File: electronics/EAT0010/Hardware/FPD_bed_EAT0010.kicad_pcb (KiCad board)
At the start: 2 copper layers, 29.2 x 48.2 mm, 20 parts, among them CN1 CONN_02X08, CN2 OSTTA060161, Q1 IPD30N03S4L-09, U1 MIC5205-5.0MB5, U2 PIC16F1704

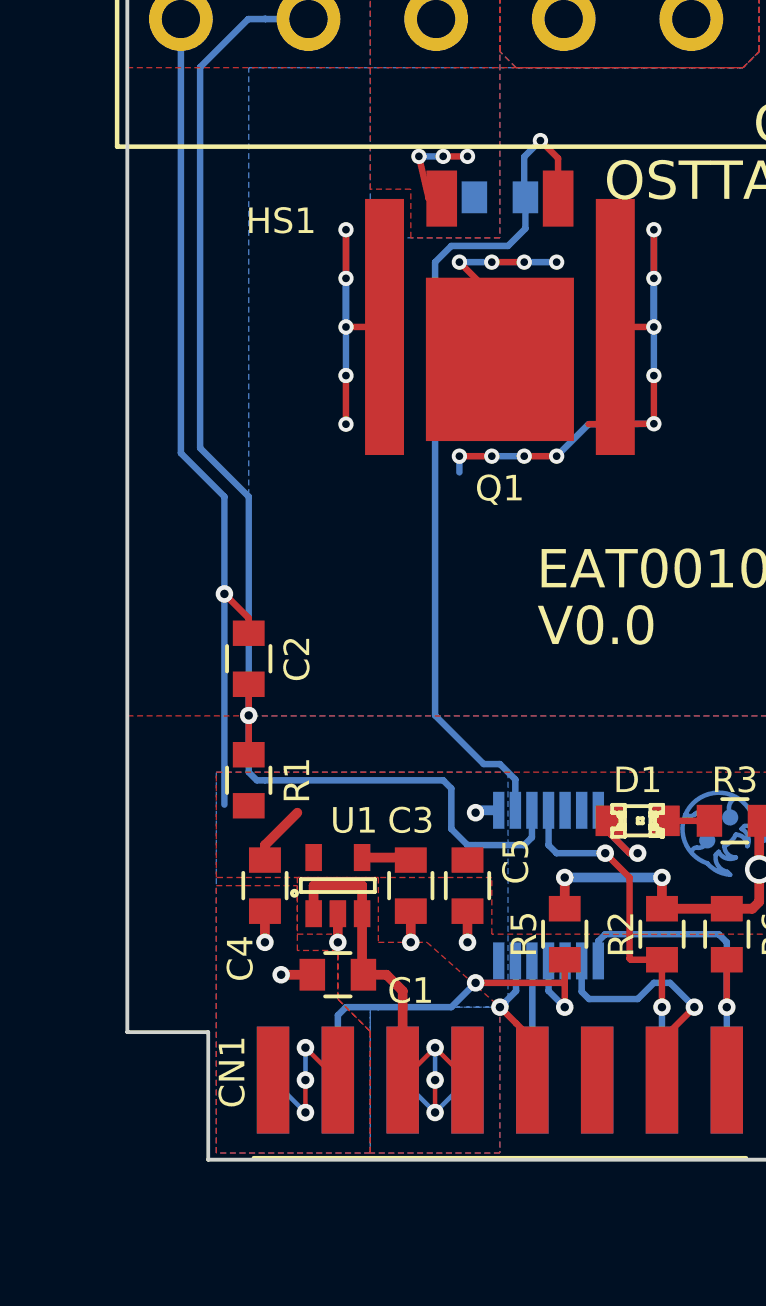
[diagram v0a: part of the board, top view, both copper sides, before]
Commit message: PCB updates
Added thermals and slid parts around a bit for better spacing
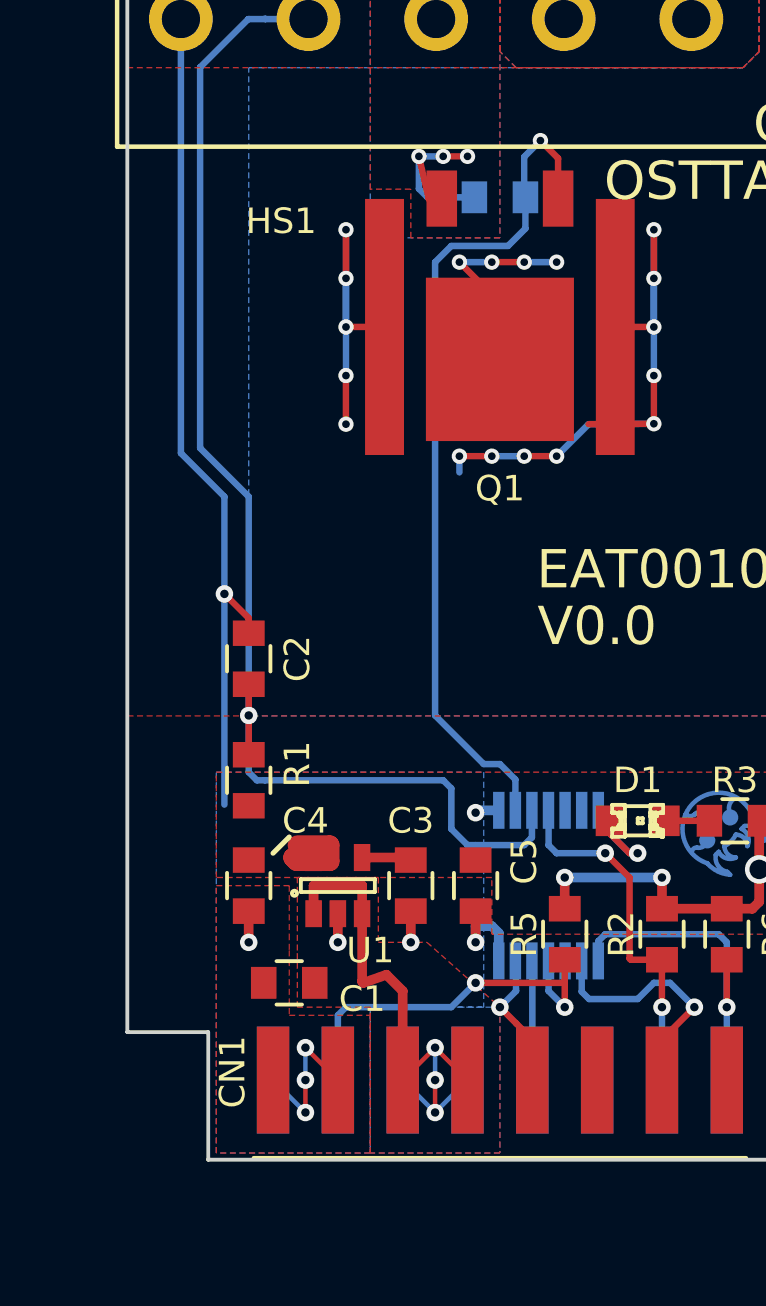
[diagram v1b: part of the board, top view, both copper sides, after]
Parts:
- moved C1 1.93 mm to (146.7, 128.3)
- moved C4 0.63 mm to (145.1, 124.5)
- moved C5 0.32 mm to (154.0, 124.5)
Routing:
- net Pwr_gnd: track 4.11 -> 7.70 mm
- net +5V: track 16.7 -> 18.5 mm
- net GND: track 45.6 -> 47.1 mm, vias 9 -> 8
